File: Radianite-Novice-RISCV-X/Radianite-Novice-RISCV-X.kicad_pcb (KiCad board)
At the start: 2 copper layers, 68.6 x 53.3 mm, 157 parts, among them J1 USB_C_Receptacle_USB2.0_16P, J2 Conn_01x10_Pin, J3 Conn_01x08_Pin, J4 Conn_01x08, J5 Conn_01x06, J6 Barrel_Jack_Switch, J7 Radianite-Link, SW1 SW_Push, U1 CH32V305RBT6, U2 ESP32-C3-WROOM-02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

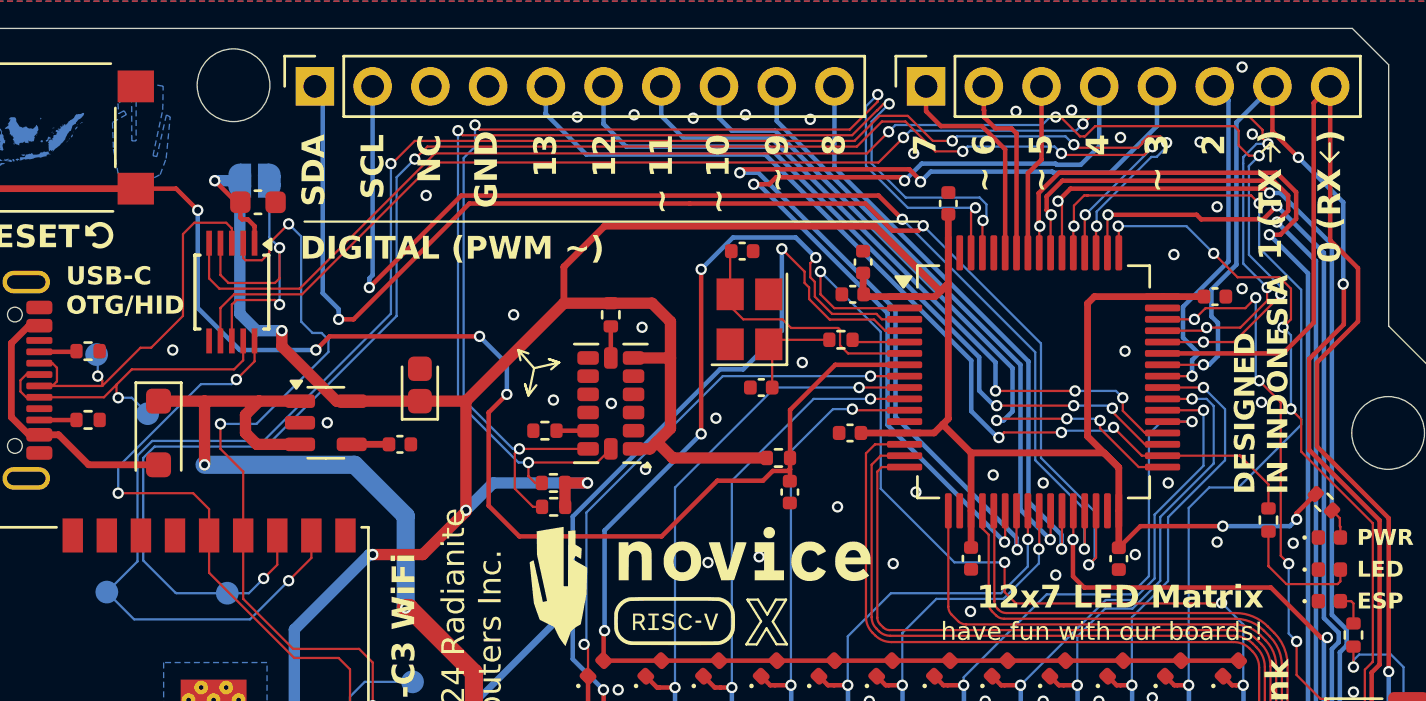
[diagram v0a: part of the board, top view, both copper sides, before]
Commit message: fixed some data lines not abiding by the clearance (make it close)
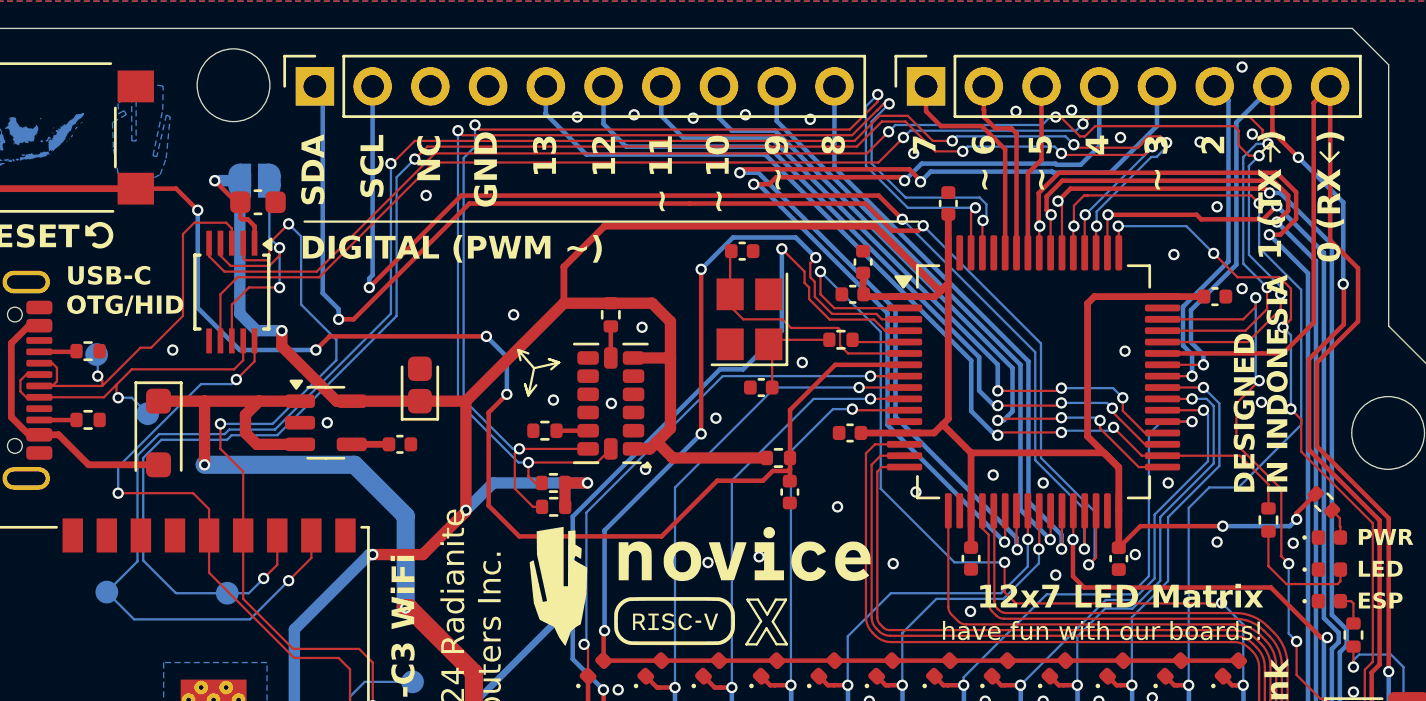
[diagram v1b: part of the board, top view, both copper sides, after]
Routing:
- net Net-(JP1-A): track 15.1 -> 12.8 mm
- net /PROG_DIO: track 31.5 -> 32.6 mm, vias 5 -> 4
- net /RV_DM: track 65.5 -> 64.7 mm, vias 5 -> 4
- net /ESP_DM: track 34.7 -> 35.3 mm
- net /RV_DP: track 65.0 -> 65.5 mm, vias 5 -> 4
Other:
- copper layers 2 -> 11
